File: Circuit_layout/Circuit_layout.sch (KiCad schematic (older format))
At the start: 19 parts, among them U7 AT90CAN128-A, U9 TLP293, Y1 10MHz

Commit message: took notes w/ greg
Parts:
- gave numbers to parts that had none: 5
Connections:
- net IMD: now also U17.6 (-), U17.7; no longer U17.1, U17.2 (-)
- net at C4.2, R5.2: now also U17.5 (+); no longer U17.3 (+)
- no-connect marks 0 -> 32
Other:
- note added: "Add Bypass Caps"
- note added: "Add Bypass Caps\n\nAdd Mounting Holes"
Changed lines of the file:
@@
 Wire Wire Line
 	6350 1100 5950 1100
-Text Label 5950 1100 0    60   ~ 0
-AIRs+_in
-Text Label 5950 1300 0    60   ~ 0
-AIRs-_in
 $Comp
 L R R7
@@
 $EndComp
 $Comp
-L MCP6004 U?
+L MCP6004 U17
 U 1 1 58B3FEE2
 P 2200 3650
-F 0 "U?" H 2250 3850 50  0000 C CNN
+F 0 "U17" H 2250 3850 50  0000 C CNN
 F 1 "MCP6004" H 2350 3450 50  0000 C CNN
 F 2 "Housings_SOIC:SOIC-14_3.9x8.7mm_Pitch1.27mm" H 2150 3750 50  0001 C CNN
@@
 $EndComp
 $Comp
-L C C?
+L C C2
 U 1 1 58B40314
 P 1150 4050
-F 0 "C?" H 1175 4150 50  0000 L CNN
+F 0 "C2" H 1175 4150 50  0000 L CNN
 F 1 "0.1u" H 1175 3950 50  0000 L CNN
 F 2 "Capacitors_SMD:C_0805_HandSoldering" H 1188 3900 50  0001 C CNN
@@
 $EndComp
 $Comp
-L C C?
+L C C1
 U 1 1 58B40445
 P 1150 3250
-F 0 "C?" H 1175 3350 50  0000 L CNN
+F 0 "C1" H 1175 3350 50  0000 L CNN
 F 1 "0.1u" H 1175 3150 50  0000 L CNN
 F 2 "Capacitors_SMD:C_0805_HandSoldering" H 1188 3100 50  0001 C CNN
@@
 $EndComp
 $Comp
-L MCP6004 U?
-U 1 1 58B40627
+L MCP6004 U17
+U 2 1 58B40627
 P 2600 1350
-F 0 "U?" H 2650 1550 50  0000 C CNN
+F 0 "U17" H 2650 1550 50  0000 C CNN
 F 1 "MCP6004" H 2750 1150 50  0000 C CNN
 F 2 "Housings_SOIC:SOIC-14_3.9x8.7mm_Pitch1.27mm" H 2550 1450 50  0001 C CNN
@@
 F 5 "http://www.digikey.com/product-detail/en/microchip-technology/MCP6004T-I-SL/MCP6004T-I-SLCT-ND/5013527" H 2600 1350 60  0001 C CNN "URL"
 F 6 "MCP6004T-I/SL" H 2600 1350 60  0001 C CNN "Man P/N"
-	1    2600 1350
-	1    0    0    -1
-$EndComp
-$Comp
-L C C?
+	2    2600 1350
+	1    0    0    -1
+$EndComp
+$Comp
+L C C4
 U 1 1 58B40E21
 P 2700 900
-F 0 "C?" H 2725 1000 50  0000 L CNN
+F 0 "C4" H 2725 1000 50  0000 L CNN
 F 1 "0.47u" H 2725 800 50  0000 L CNN
 F 2 "Capacitors_SMD:C_0805_HandSoldering" H 2738 750 50  0001 C CNN
@@
 $EndComp
 $Comp
-L C C?
+L C C5
 U 1 1 58B423A5
 P 2750 2900
-F 0 "C?" H 2775 3000 50  0000 L CNN
+F 0 "C5" H 2775 3000 50  0000 L CNN
 F 1 "10p" H 2775 2800 50  0000 L CNN
 F 2 "Capacitors_SMD:C_0805_HandSoldering" H 2788 2750 50  0001 C CNN
@@
 Wire Wire Line
 	9850 4000 9700 4000
+Text Notes 3100 5900 0    60   ~ 0
+Add Bypass Caps\n\nAdd Mounting Holes
+Text Notes 3000 700  0    60   ~ 0
+Add Bypass Caps
+NoConn ~ 6550 2100
+NoConn ~ 6550 2200
+NoConn ~ 6550 2600
+NoConn ~ 6550 2700
+NoConn ~ 6550 2900
+NoConn ~ 6550 3000
+NoConn ~ 6550 3100
+NoConn ~ 6550 3200
+NoConn ~ 6550 3800
+NoConn ~ 6550 4200
+NoConn ~ 6550 4300
+NoConn ~ 6550 4400
+NoConn ~ 6550 4500
+NoConn ~ 6550 4700
+NoConn ~ 6550 4800
+NoConn ~ 6550 4900
+NoConn ~ 6550 5000
+NoConn ~ 6550 5100
+NoConn ~ 3950 5400
+NoConn ~ 3950 5300
+NoConn ~ 3950 5200
+NoConn ~ 3950 5100
+NoConn ~ 3950 5000
+NoConn ~ 3950 4900
+NoConn ~ 3950 4800
+NoConn ~ 3950 4700
+NoConn ~ 3950 3200
+NoConn ~ 3950 3300
+NoConn ~ 3950 3400
+NoConn ~ 3950 3500
+NoConn ~ 3950 3600
+Text GLabel 5950 1100 0    60   Input ~ 0
+AIRs+_in
+Text GLabel 5950 1300 0    60   Input ~ 0
+AIRs-_in
+NoConn ~ 6550 5400
 $EndSCHEMATC

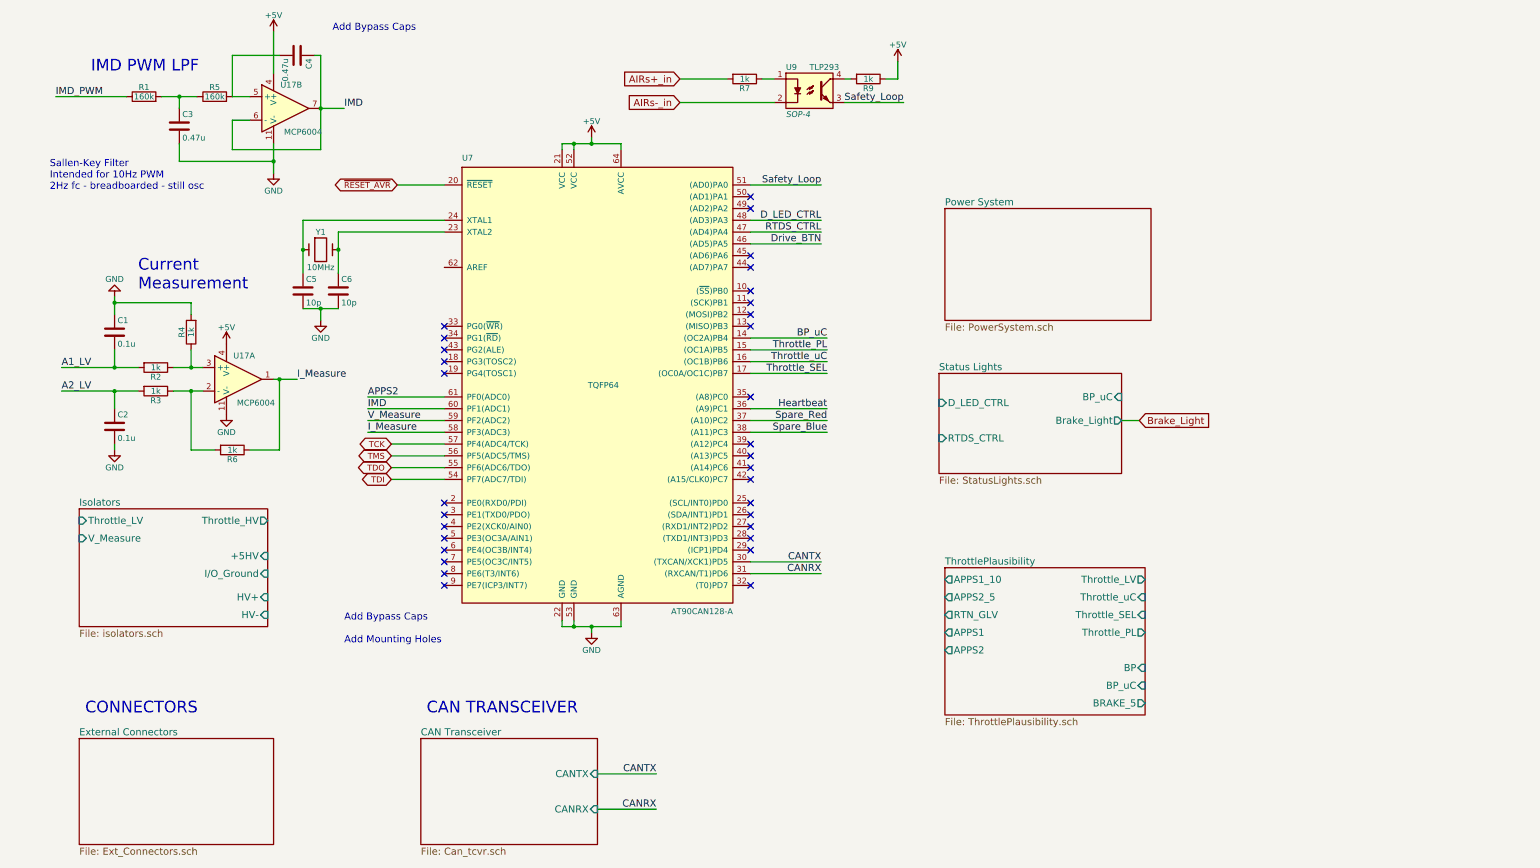
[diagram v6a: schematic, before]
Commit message: got rid of some warnings with nets.
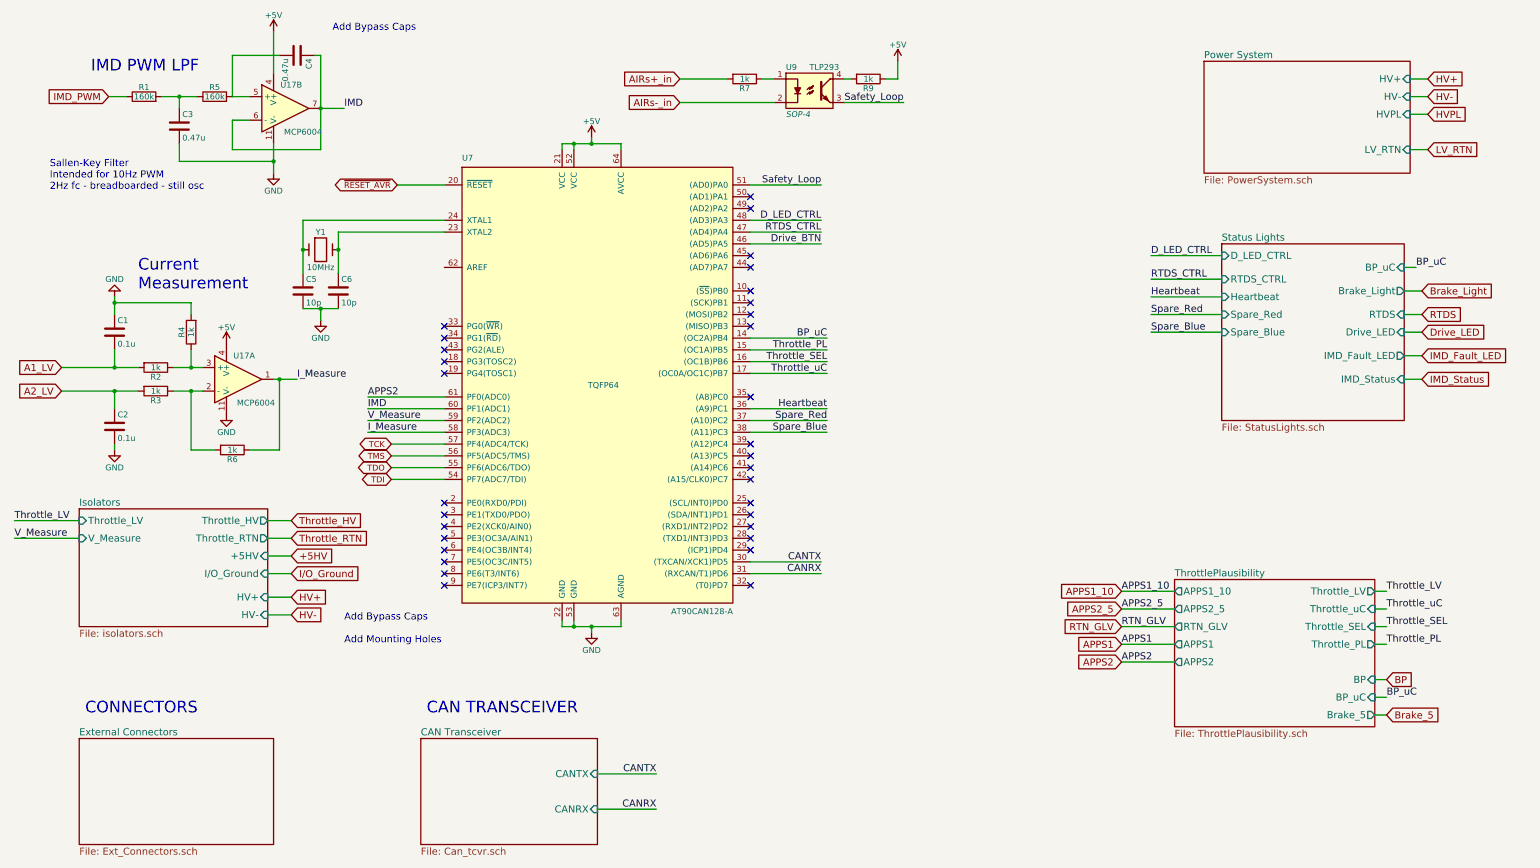
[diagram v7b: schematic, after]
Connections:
- net Throttle_SEL: now also U7.16 ((OC1B)PB6); no longer U7.17 ((OC0A/OC1C)PB7)
- net Throttle_uC: now also U7.17 ((OC0A/OC1C)PB7); no longer U7.16 ((OC1B)PB6)

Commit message: eliminated warnings, need to clean things up + add footprints/datasheets
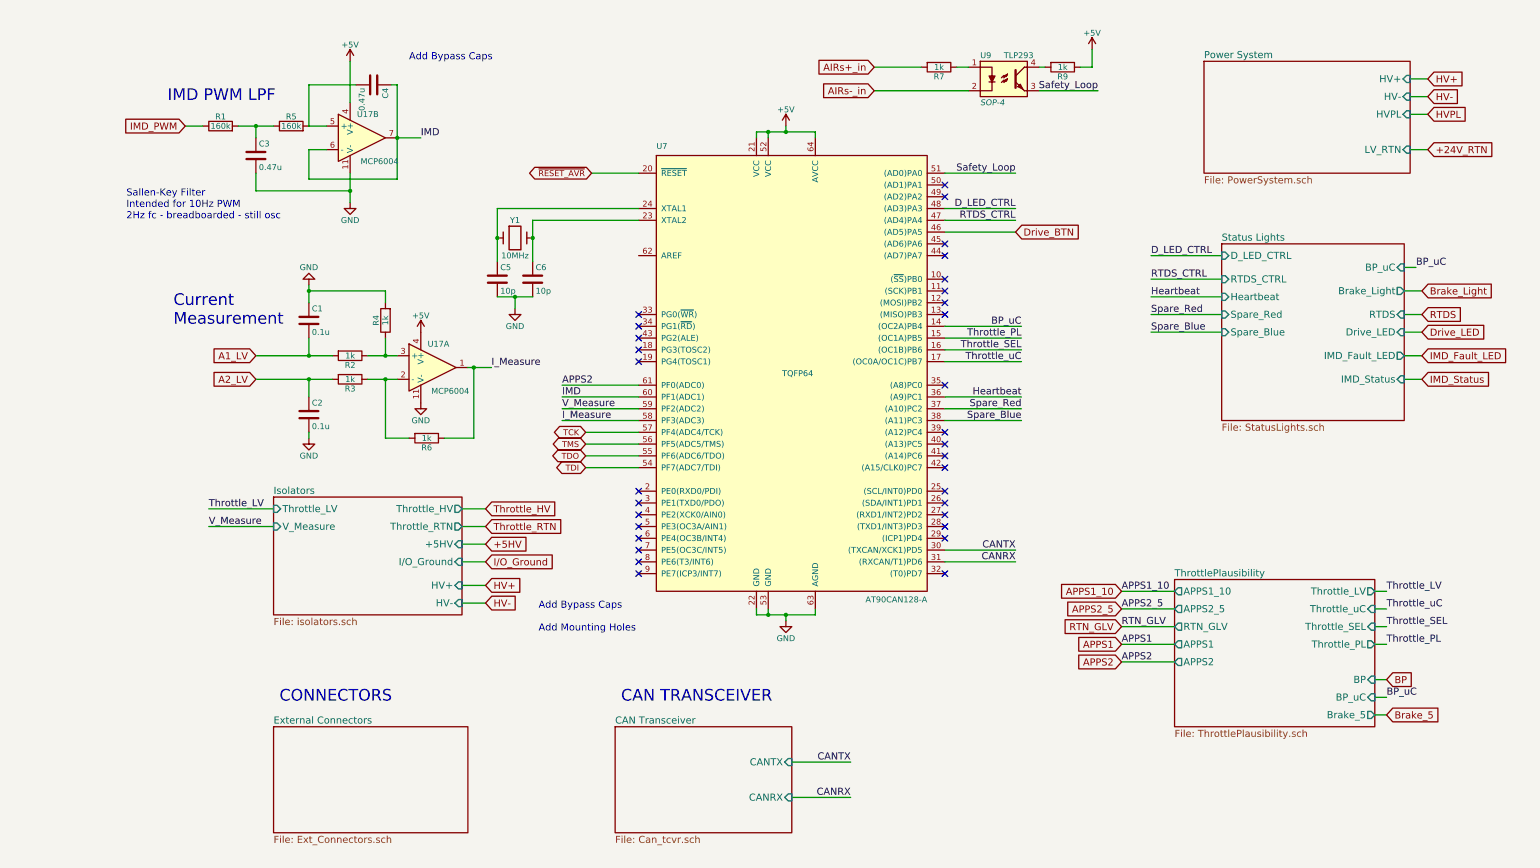
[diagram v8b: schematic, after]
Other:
- moved on the sheet: C1, C2, C3, C4, C5, C6, R1, R2, R3, R4, R5, R6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
